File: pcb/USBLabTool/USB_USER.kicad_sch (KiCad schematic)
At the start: 20 parts, among them J20 USB_C_Receptacle, Q1 STL11N3LLH6, U17 TCPP01-M12, U19 USBLC6-2SC6

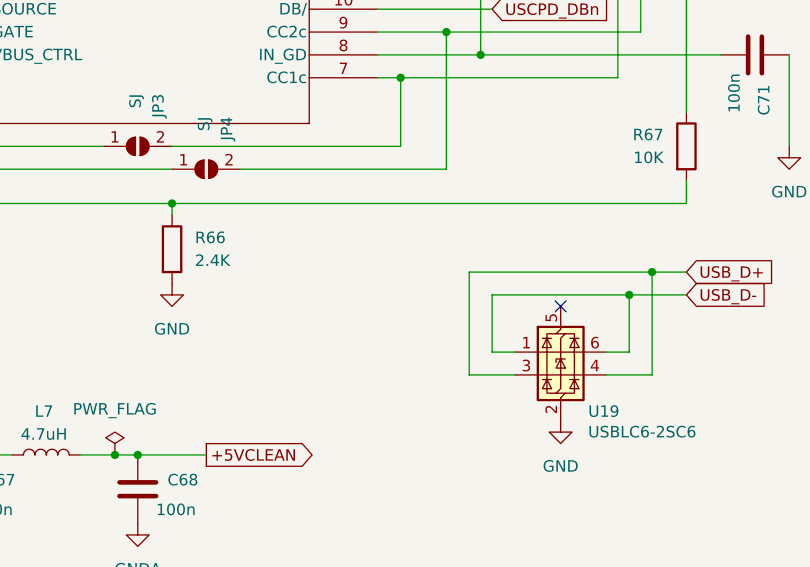
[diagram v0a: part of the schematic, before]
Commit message: nearly finish MCU, need checking, and unfinished logic analyzer
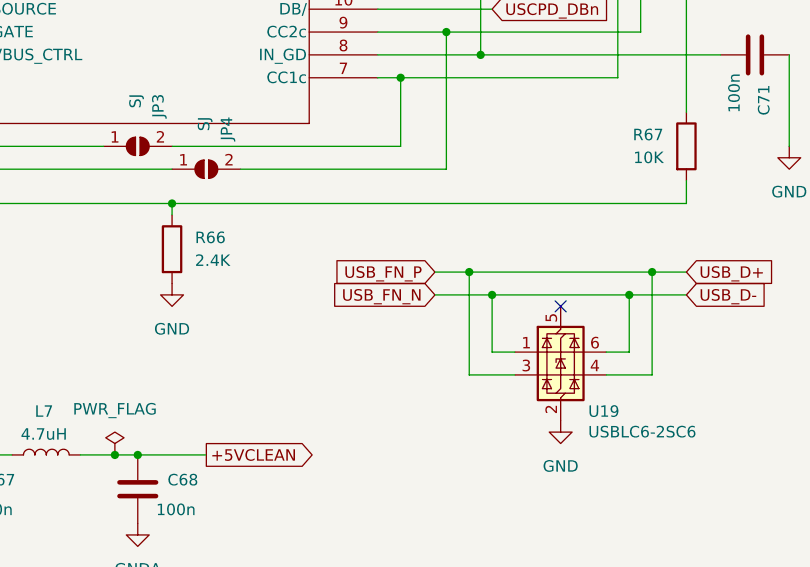
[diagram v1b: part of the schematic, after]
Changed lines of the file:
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@@
+	)
+	(junction
+		(at 153.67 124.46)
+		(diameter 0)
+		(color 0 0 0 0)
 	)
 	(junction
@@
 	(junction
 		(at 148.59 95.25)
+		(diameter 0)
+		(color 0 0 0 0)
+	)
+	(junction
+		(at 151.13 121.92)
 		(diameter 0)
 		(color 0 0 0 0)
@@
 	(wire
 		(pts
+			(xy 147.32 124.46) (xy 153.67 124.46)
+		)
+		(stroke
+			(width 0)
+			(type default)
+		)
+	)
+	(wire
+		(pts
 			(xy 152.4 97.79) (xy 179.07 97.79)
 		)
@@
 		(pts
 			(xy 140.97 90.17) (xy 154.94 90.17)
+		)
+		(stroke
+			(width 0)
+			(type default)
+		)
+	)
+	(wire
+		(pts
+			(xy 147.32 121.92) (xy 151.13 121.92)
 		)
 		(stroke
@@
 		)
 	)
+	(global_label "USB_FN_P"
+		(shape input)
+		(at 147.32 121.92 180)
+		(fields_autoplaced yes)
+		(effects
+			(font
+				(size 1.27 1.27)
+			)
+			(justify right)
+		)
+		(property "Intersheetrefs" "${INTERSHEET_REFS}"
+			(at 134.9005 121.92 0)
+			(effects
+				(font
+					(size 1.27 1.27)
+				)
+				(justify right)
+				(hide yes)
+			)
+		)
+	)
 	(global_label "UCPD_CC2"
 		(shape input)
@@
 			(effects
 				(font
+					(size 1.27 1.27)
+				)
+				(justify right)
+				(hide yes)
+			)
+		)
+	)
+	(global_label "USB_FN_N"
+		(shape input)
+		(at 147.32 124.46 180)
+		(fields_autoplaced yes)
+		(effects
+			(font
+				(size 1.27 1.27)
+			)
+			(justify right)
+		)
+		(property "Intersheetrefs" "${INTERSHEET_REFS}"
+			(at 134.84 124.46 0)
+			(effects
+				(font
